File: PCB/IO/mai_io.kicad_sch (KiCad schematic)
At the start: 43 parts, among them J1 Conn_01x34_Female, U1 Pico, U2 MPR121QR2, U3 MPR121QR2, U4 MPR121QR2, U5 MPR121QR2_BOARD, U6 MPR121QR2_BOARD, U7 MPR121QR2_BOARD, U8 SN74LV1T34DBV

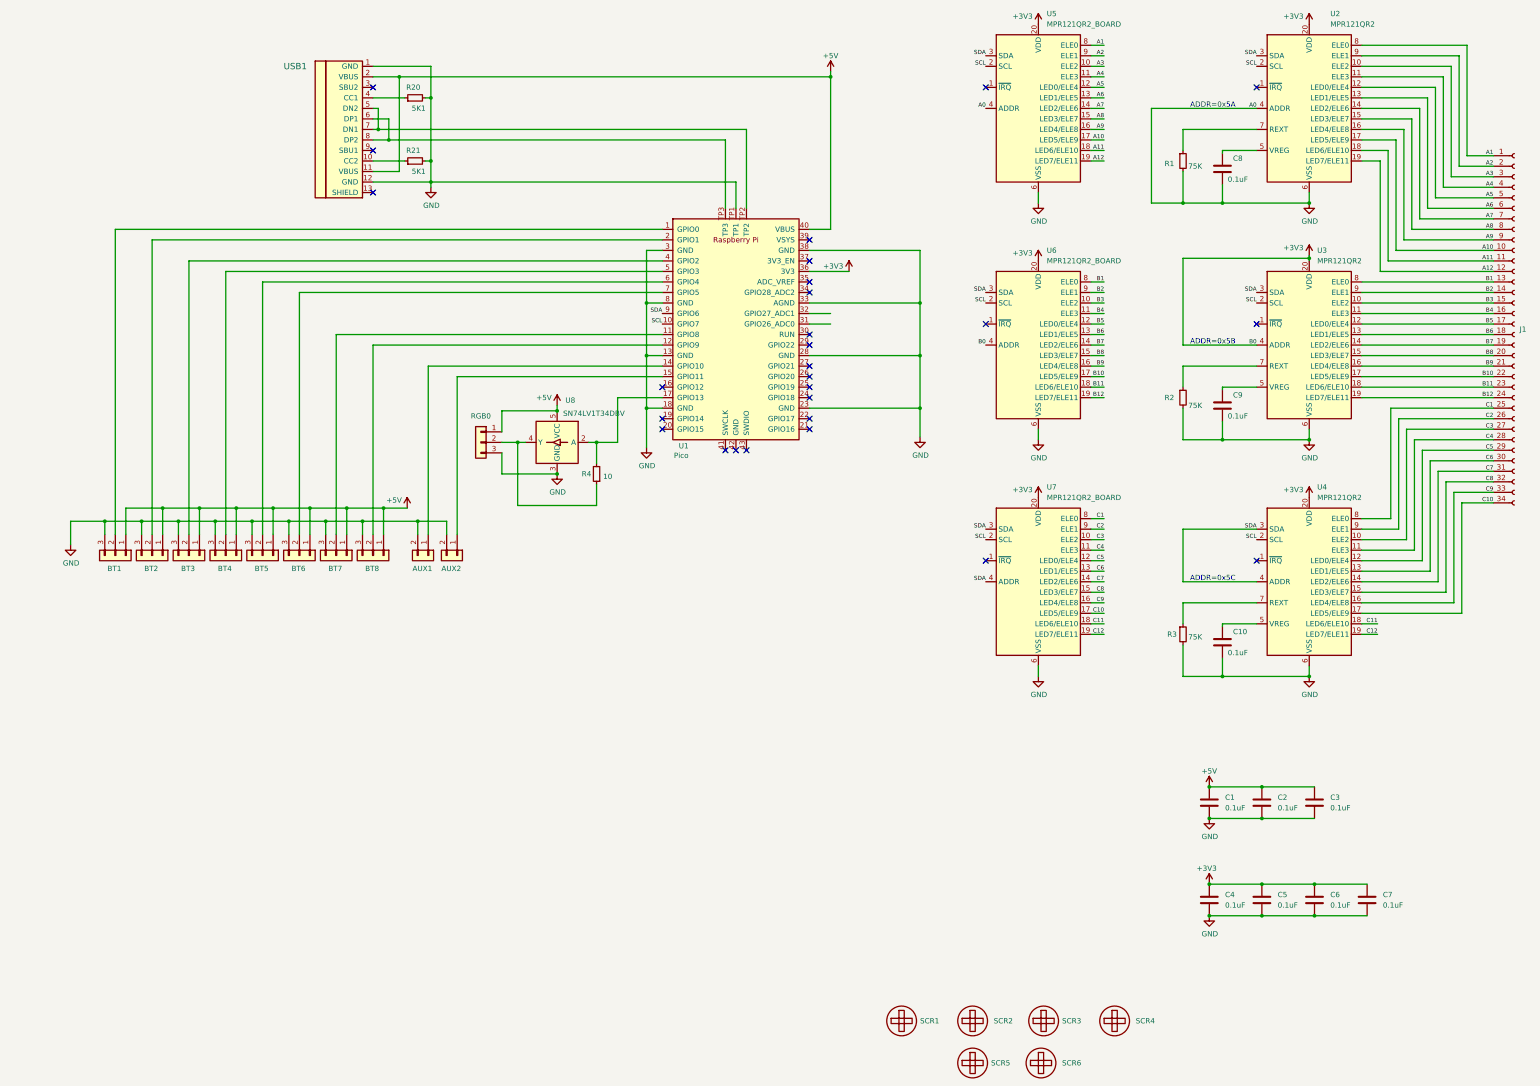
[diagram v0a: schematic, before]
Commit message: IO board v1.1 (better support for arcade buttons and simplified)
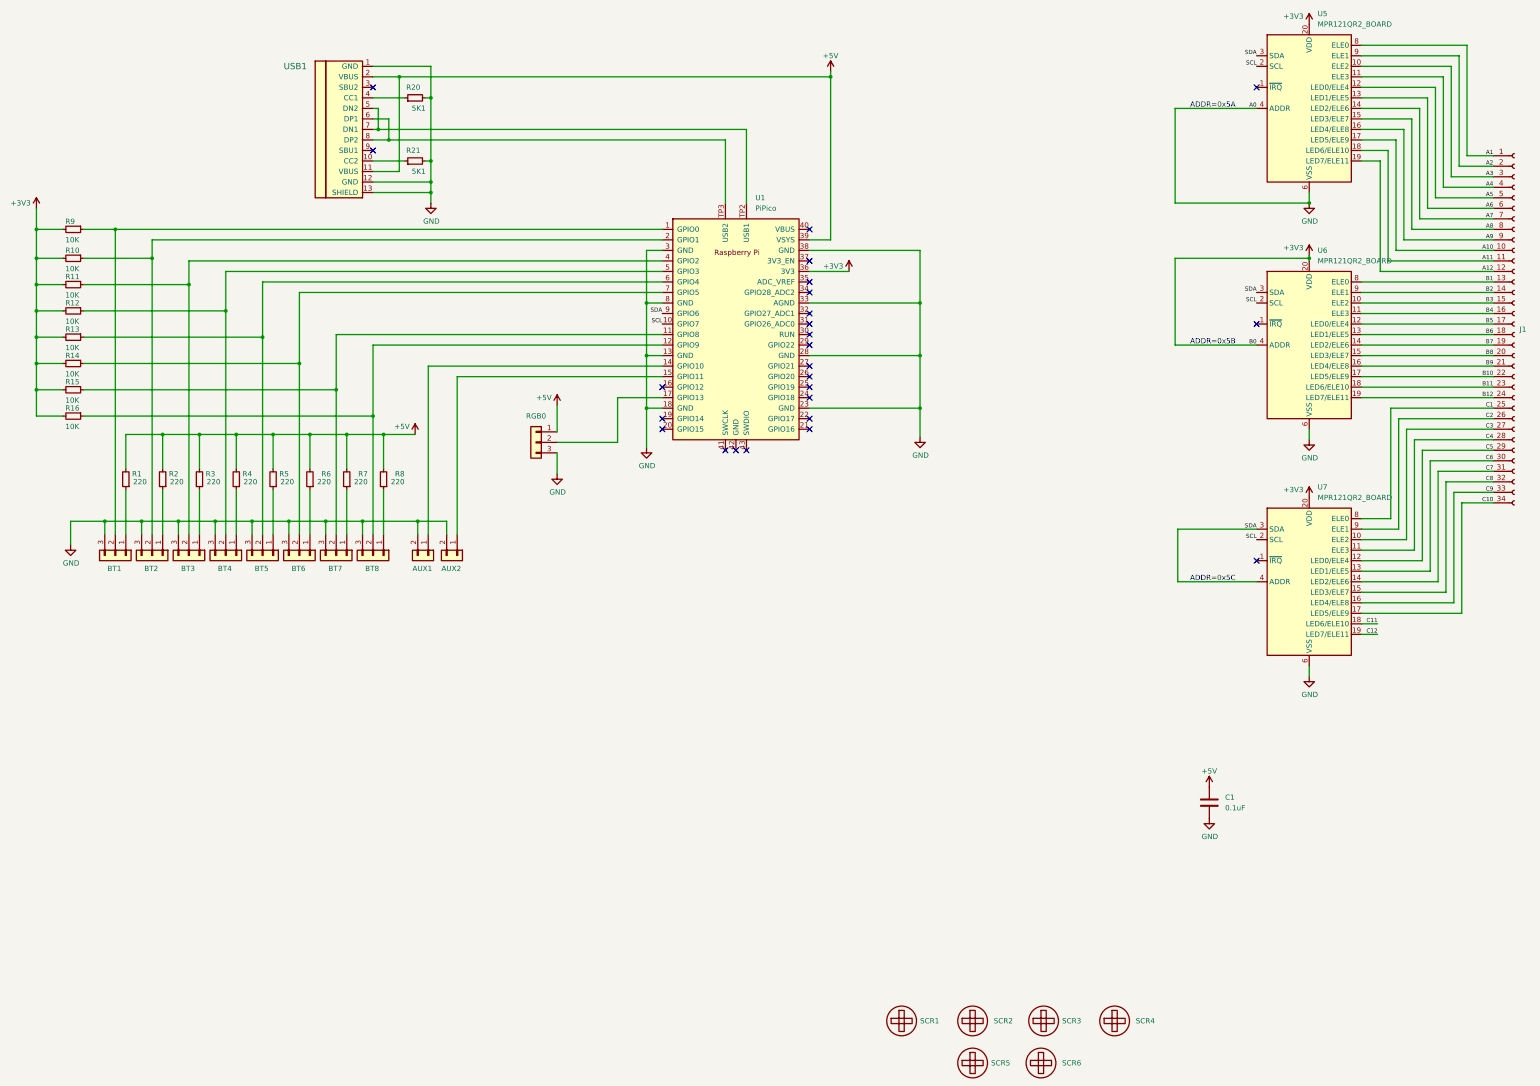
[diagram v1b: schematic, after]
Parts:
- removed C10, C2, C3, C4, C5, C6, C7, C8, C9: 0.1uF, Capacitor_SMD:C_0603_1608Metric_Pad1.08x0.95mm_HandSolder, symbol Device:C
- removed U1: Pico, mai_io:RPi_Pico_SMD_Pins, symbol MCU_RaspberryPi_and_Boards:Pico
- removed U2, U3, U4: MPR121QR2, Package_DFN_QFN:UQFN-20_3x3mm_P0.4mm, symbol Sensor_Touch:MPR121QR2
- removed U8: SN74LV1T34DBV, mai_io:SOT-23-5_Jumper, symbol Logic_LevelTranslator:SN74LV1T34DBV
- added R10, R11, R12, R13, R14, R15, R16, R9: 10K, Resistor_SMD:R_0603_1608Metric_Pad0.98x0.95mm_HandSolder, symbol Device:R_Small
- added R5, R6, R7, R8: 220, Resistor_SMD:R_0603_1608Metric_Pad0.98x0.95mm_HandSolder, symbol Device:R_Small
- added U1: PiPico, mai_io:RPi_Pico_SMD_Pins, symbol mai_io:PiPico
- R1, R2, R3: value 75K -> 220; footprint Resistor_SMD:R_0603_1608Metric -> Resistor_SMD:R_0603_1608Metric_Pad0.98x0.95mm_HandSolder
- R20, R21: footprint Resistor_SMD:R_0603_1608Metric -> Resistor_SMD:R_0603_1608Metric_Pad0.98x0.95mm_HandSolder
- R4: value 10 -> 220; footprint Resistor_SMD:R_0603_1608Metric -> Resistor_SMD:R_0603_1608Metric_Pad0.98x0.95mm_HandSolder
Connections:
- net +3V3: now also R10.2, R11.2, R12.2, R13.2, R14.2, R15.2, R16.2, R9.2, U1.36 (3V3)
- net +5V: now also R1.2, R2.2, R3.2, R4.2, R5.2, R6.2, R7.2, R8.2, U1.39 (VSYS); no longer BT1.1 (Pin_1), BT2.1 (Pin_1), BT3.1 (Pin_1), BT4.1 (Pin_1), BT5.1 (Pin_1), BT6.1 (Pin_1), BT7.1 (Pin_1), BT8.1 (Pin_1)
- net GND: now also USB1.13 (SHIELD), U1.13 (GND), U1.18 (GND), U1.23 (GND), U1.28 (GND), U1.3 (GND), U1.33 (AGND), U1.38 (GND), U1.8 (GND); no longer R1.2, R2.2, R3.2
- net SCL: now also U1.10 (GPIO7)
- net SDA: now also U1.9 (GPIO6)
- net at BT1.2 (Pin_2): now also R9.1, U1.1 (GPIO0)
- net at BT7.2 (Pin_2): now also R15.1, U1.11 (GPIO8)
- net at BT8.2 (Pin_2): now also R16.1, U1.12 (GPIO9)
- net at AUX1.1 (Pin_1): now also U1.14 (GPIO10)
- net at AUX2.1 (Pin_1): now also U1.15 (GPIO11)
- net at BT2.2 (Pin_2): now also R10.1, U1.2 (GPIO1)
- net at BT3.2 (Pin_2): now also R11.1, U1.4 (GPIO2)
- net at BT4.2 (Pin_2): now also R12.1, U1.5 (GPIO3)
- net at BT5.2 (Pin_2): now also R13.1, U1.6 (GPIO4)
- net at BT6.2 (Pin_2): now also R14.1, U1.7 (GPIO5)
- net at USB1.5 (DN2), USB1.7 (DN1): now also U1.TP2 (USB1)
- net at USB1.6 (DP1), USB1.8 (DP2): now also U1.TP3 (USB2)
- net at R2.1: now also BT2.1 (Pin_1)
- net at R4.1: now also BT4.1 (Pin_1); no longer RGB0.2 (Pin_2)
- net at R1.1: now also BT1.1 (Pin_1)
- net at R3.1: now also BT3.1 (Pin_1)
- new net: BT5.1 (Pin_1), R5.1
- new net: RGB0.2 (Pin_2), U1.17 (GPIO13)
- new net: BT8.1 (Pin_1), R8.1
- new net: BT6.1 (Pin_1), R6.1
- new net: BT7.1 (Pin_1), R7.1
- no-connect marks 27 -> 25
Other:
- moved on the sheet: RGB0, U5, U6, U7
